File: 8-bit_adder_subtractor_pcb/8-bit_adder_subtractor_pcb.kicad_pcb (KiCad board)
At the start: 2 copper layers, 158.7 x 142 mm, 86 parts, among them J1 Barrel_Jack, SW1 SW_DPDT_x2, SW10 SW_DPDT_x2, SW11 SW_DPDT_x2, SW12 SW_DPDT_x2, SW13 SW_DPDT_x2, SW14 SW_DPDT_x2, SW15 SW_DPDT_x2, SW16 SW_DPDT_x2, SW17 SW_DPDT_x2, SW2 SW_DPDT_x2, SW3 SW_DPDT_x2, SW4 SW_DPDT_x2, SW5 SW_DPDT_x2, SW6 SW_DPDT_x2, SW7 SW_DPDT_x2, SW8 SW_DPDT_x2, SW9 SW_DPDT_x2, U1 74LS86, U10 74LS86, U11 74LS08, U12 74LS32, U2 74LS86, U3 74LS08, U4 74LS08, U5 74LS32, U6 74LS86, U7 74LS86, U8 74LS86, U9 74LS08

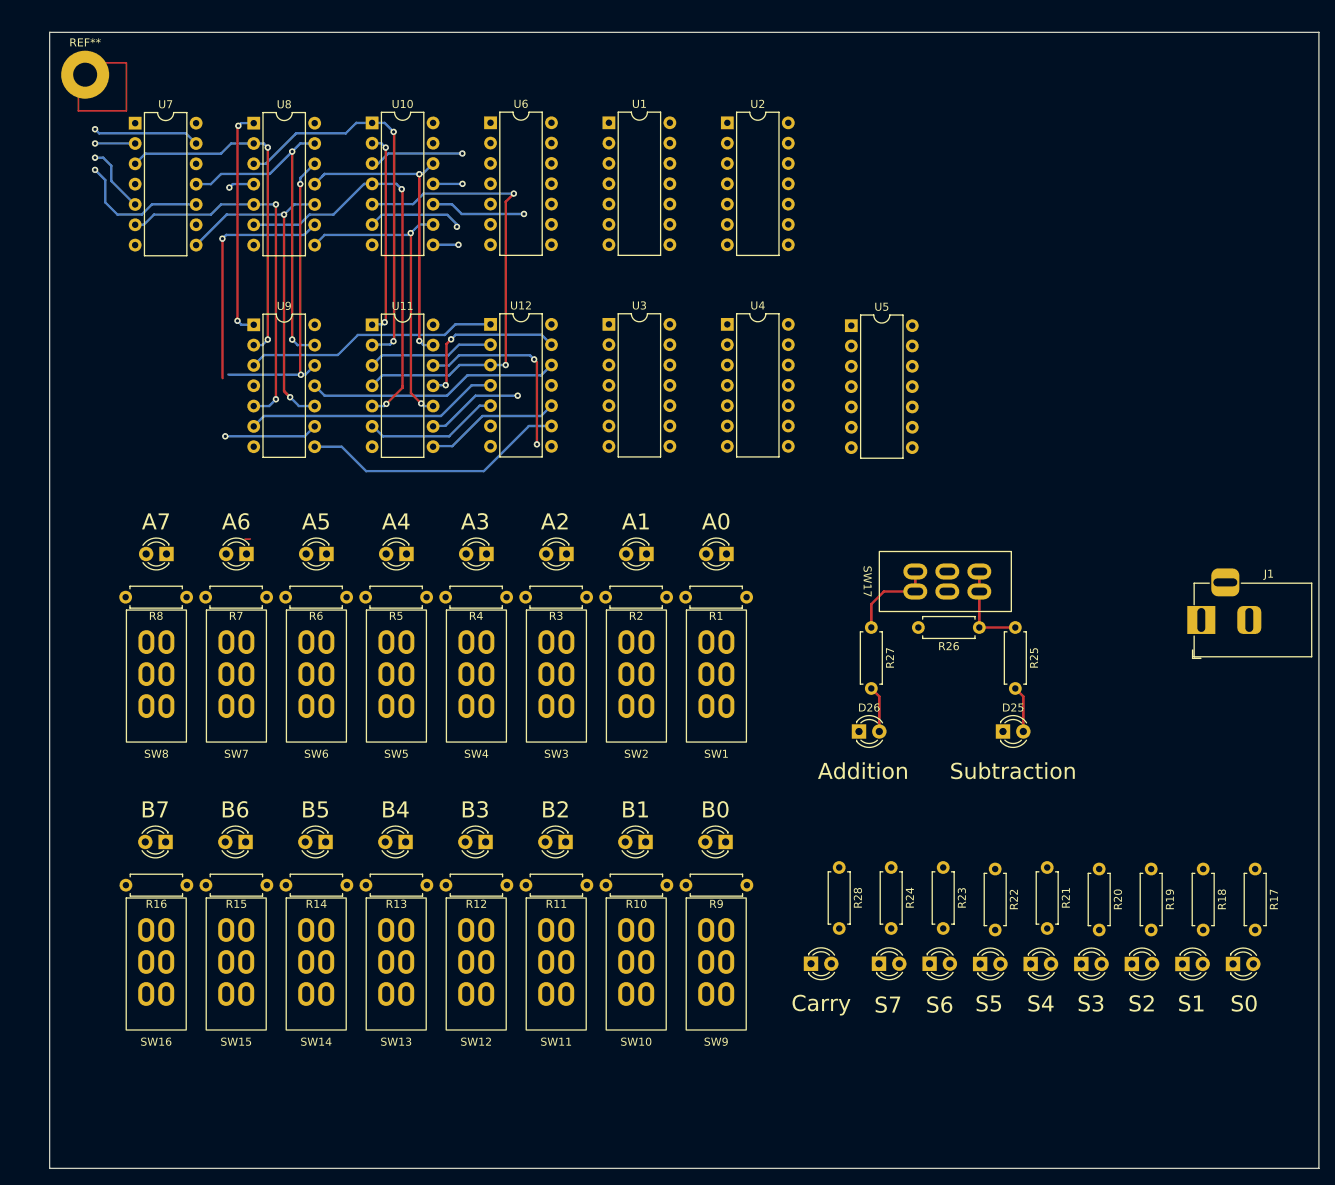
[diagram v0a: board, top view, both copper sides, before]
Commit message: Edited the Silkscreen for LAB448
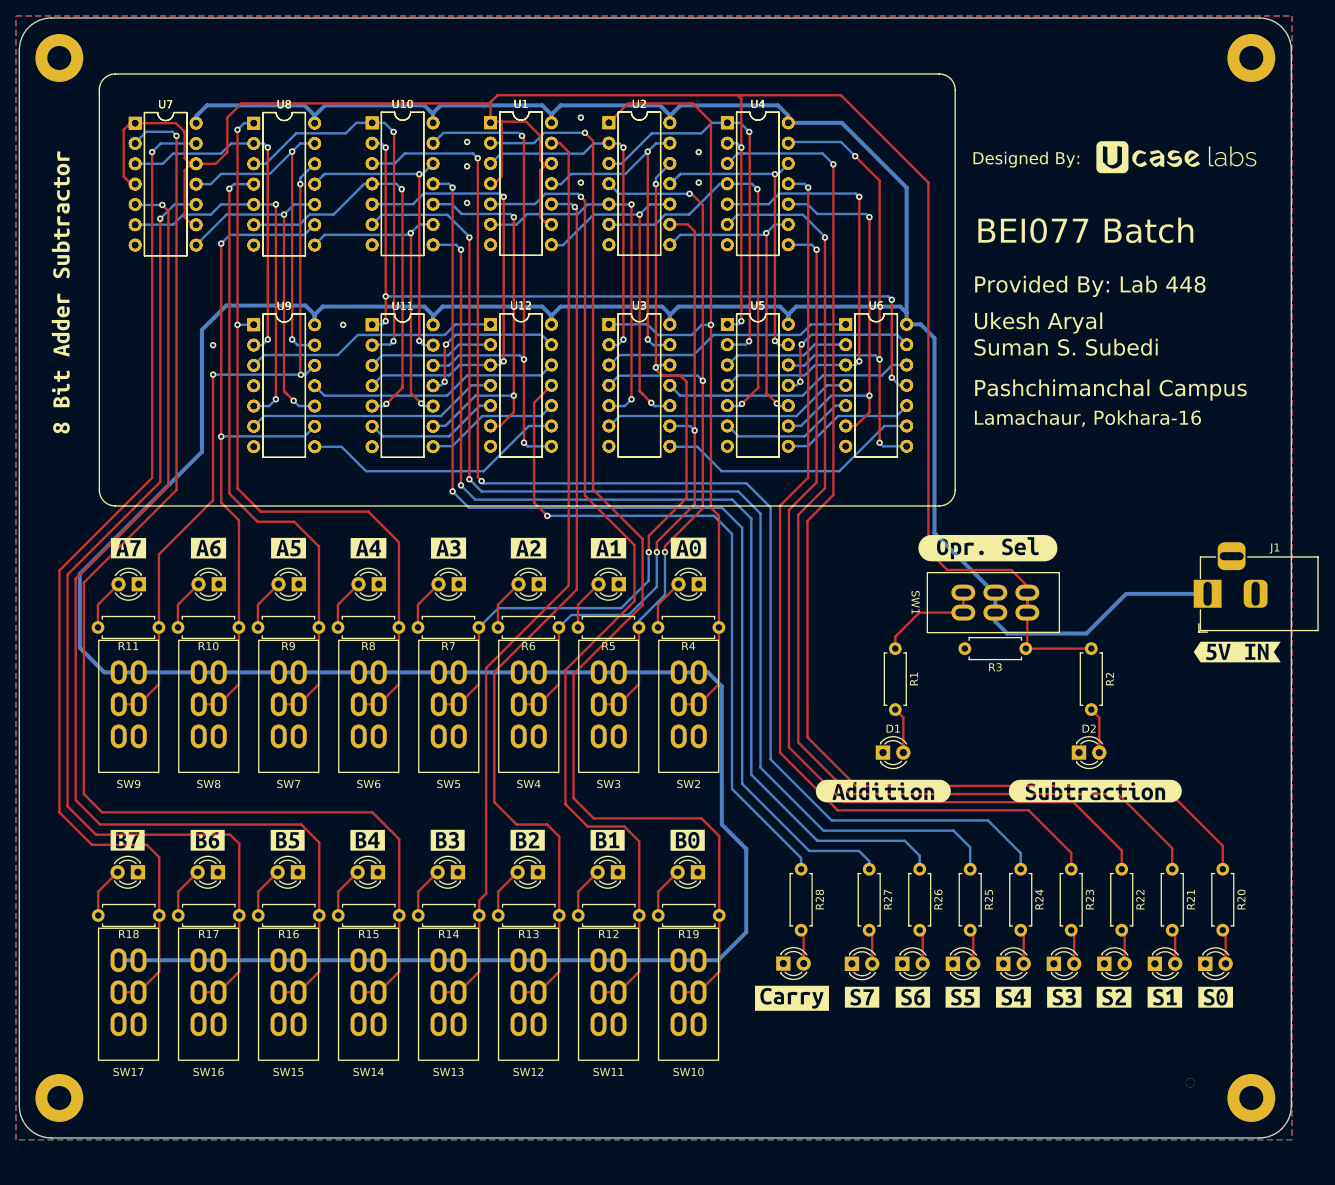
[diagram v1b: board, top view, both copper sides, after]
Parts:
- removed the REF** at (20.7, 15.5)
- added G***: LOGO, Assets:logo, F.Cu at (157.1, 26.2)
- added G***: LOGO, Assets:logo, B.Cu at (150.0, 18.4)
- added H1: MountingHole_Pad, MountingHole:MountingHole_3mm_Pad, F.Cu at (17.5, 13.4)
- added H2: MountingHole_Pad, MountingHole:MountingHole_3mm_Pad, F.Cu at (166.5, 13.4)
- added H3: MountingHole_Pad, MountingHole:MountingHole_3mm_Pad, F.Cu at (166.5, 143.4)
- added H4: MountingHole_Pad, MountingHole:MountingHole_3mm_Pad, F.Cu at (17.5, 143.4)
- added REF**: JLCPC_1.152 Tooling hole, Assets:JLCPC_1.152 Tooling hole, F.Cu at (159.4, 144.6)
- added U1: 74LS86, Package_DIP:DIP-14_W7.62mm, F.Cu at (71.4, 21.6)
- added U10: 74LS86, Package_DIP:DIP-14_W7.62mm, F.Cu at (56.6, 21.6)
- added U11: 74LS08, Package_DIP:DIP-14_W7.62mm, F.Cu at (56.6, 46.8)
- added U12: 74LS32, Package_DIP:DIP-14_W7.62mm, F.Cu at (71.4, 46.8)
- added U2: 74LS86, Package_DIP:DIP-14_W7.62mm, F.Cu at (86.2, 21.6)
- added U3: 74LS08, Package_DIP:DIP-14_W7.62mm, F.Cu at (86.2, 46.8)
- added U4: 74LS86, Package_DIP:DIP-14_W7.62mm, F.Cu at (101.0, 21.6)
- added U5: 74LS08, Package_DIP:DIP-14_W7.62mm, F.Cu at (101.0, 46.8)
- added U6: 74LS32, Package_DIP:DIP-14_W7.62mm, F.Cu at (115.8, 46.8)
- added U7: 74LS86, Package_DIP:DIP-14_W7.62mm, F.Cu at (27.0, 21.6)
- added U8: 74LS86, Package_DIP:DIP-14_W7.62mm, F.Cu at (41.8, 21.6)
- added U9: 74LS08, Package_DIP:DIP-14_W7.62mm, F.Cu at (41.8, 46.8)
- added kibuzzard-6723279E: G***, kibuzzard-6723279E, F.Cu at (86.2, 74.7)
- added kibuzzard-672327BC: G***, kibuzzard-672327BC, F.Cu at (26.2, 74.7)
- added kibuzzard-672327C5: G***, kibuzzard-672327C5, F.Cu at (36.2, 74.7)
- added kibuzzard-672327D0: G***, kibuzzard-672327D0, F.Cu at (46.2, 74.7)
- added kibuzzard-672327D8: G***, kibuzzard-672327D8, F.Cu at (56.2, 74.7)
- added kibuzzard-672327DE: G***, kibuzzard-672327DE, F.Cu at (66.2, 74.7)
- added kibuzzard-672327E5: G***, kibuzzard-672327E5, F.Cu at (76.2, 74.7)
- added kibuzzard-672327EF: G***, kibuzzard-672327EF, F.Cu at (96.2, 74.7)
- added kibuzzard-6723280D: G***, kibuzzard-6723280D, F.Cu at (120.5, 105.1)
- added kibuzzard-67232848: G***, kibuzzard-67232848, F.Cu at (147.0, 105.1)
- added kibuzzard-6723CCFE: G***, kibuzzard-6723CCFE, F.Cu at (26.0, 111.2)
- added kibuzzard-6723CD06: G***, kibuzzard-6723CD06, F.Cu at (36.0, 111.2)
- added kibuzzard-6723CD0E: G***, kibuzzard-6723CD0E, F.Cu at (46.0, 111.2)
- added kibuzzard-6723CD14: G***, kibuzzard-6723CD14, F.Cu at (56.0, 111.2)
- added kibuzzard-6723CD1A: G***, kibuzzard-6723CD1A, F.Cu at (66.0, 111.2)
- added kibuzzard-6723CD21: G***, kibuzzard-6723CD21, F.Cu at (76.0, 111.2)
- added kibuzzard-6723CD27: G***, kibuzzard-6723CD27, F.Cu at (86.0, 111.2)
- added kibuzzard-6723CD2D: G***, kibuzzard-6723CD2D, F.Cu at (96.0, 111.2)
- added kibuzzard-6723D2BC: G***, kibuzzard-6723D2BC, F.Cu at (109.1, 131.0)
- added kibuzzard-6723D2C8: G***, kibuzzard-6723D2C8, F.Cu at (117.8, 130.9)
- added kibuzzard-6723D2CE: G***, kibuzzard-6723D2CE, F.Cu at (124.2, 130.9)
- added kibuzzard-6723D2D3: G***, kibuzzard-6723D2D3, F.Cu at (130.4, 130.9)
- added kibuzzard-6723D2DF: G***, kibuzzard-6723D2DF, F.Cu at (136.8, 130.9)
- added kibuzzard-6723D2E6: G***, kibuzzard-6723D2E6, F.Cu at (143.1, 130.9)
- added kibuzzard-6723D2EE: G***, kibuzzard-6723D2EE, F.Cu at (149.3, 130.9)
- added kibuzzard-6723D31B: G***, kibuzzard-6723D31B, F.Cu at (155.7, 130.9)
- added kibuzzard-6723D320: G***, kibuzzard-6723D320, F.Cu at (162.0, 130.9)
- added kibuzzard-6723D341: G***, kibuzzard-6723D341, F.Cu at (133.6, 74.7)
- added kibuzzard-672491A3: G***, kibuzzard-672491A3, F.Cu at (164.7, 87.7)
- added kibuzzard-68098BF2: G***, kibuzzard-68098BF2, F.Cu at (17.7, 42.7)
- moved D2 9.86 mm to (145.0, 100.3)
- moved R2 9.86 mm to (146.5, 87.3)
- moved SW1 6.56 mm to (134.5, 81.5)
- moved R3 6.38 mm to (138.3, 87.3)
- moved SW6 5.13 mm to (56.2, 94.2)
- moved SW7 5.13 mm to (46.2, 94.2)
- moved SW8 5.13 mm to (36.2, 94.2)
- moved SW17 5.13 mm to (26.2, 130.2)
- moved R10 5.13 mm to (40.0, 84.6)
- moved R12 5.13 mm to (90.0, 120.6)
- moved R13 5.13 mm to (80.0, 120.6)
- moved R14 5.13 mm to (70.0, 120.6)
- moved R15 5.13 mm to (60.0, 120.6)
- moved R16 5.13 mm to (50.0, 120.6)
- moved R17 5.13 mm to (40.0, 120.6)
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- renumbered D26 to D1, A7 to D10, B1 to D11, B2 to D12, B3 to D13, B4 to D14, B5 to D15, B6 to D16, B7 to D17, B0 to D18, S0 to D19, D25 to D2, S1 to D20, S2 to D21, S3 to D22, S4 to D23, S5 to D24, S6 to D25, S7 to D26, Carry to D27, A0 to D3, A1 to D4, A2 to D5, A3 to D6, A4 to D7, A5 to D8, A6 to D9, R27 to R1, R7 to R10, R8 to R11, R10 to R12, R11 to R13, R12 to R14, R13 to R15, R14 to R16, R15 to R17, R16 to R18, R9 to R19, R25 to R2, R17 to R20, R18 to R21, R19 to R22, R20 to R23, R21 to R24, R22 to R25, R23 to R26, R24 to R27, R26 to R3, R1 to R4, R2 to R5, R3 to R6, R4 to R7, R5 to R8, R6 to R9, SW17 to SW1, SW9 to SW10, SW10 to SW11, SW11 to SW12, SW12 to SW13, SW13 to SW14, SW14 to SW15, SW15 to SW16, SW16 to SW17, SW1 to SW2, SW2 to SW3, SW3 to SW4, SW4 to SW5, SW5 to SW6, SW6 to SW7, SW7 to SW8, SW8 to SW9, U6 to U1, U1 to U2, U2 to U4, U4 to U5, U5 to U6
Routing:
- net VCC: track 0.00 -> 541.3 mm
- net SL: track 11.5 -> 275.9 mm, vias 0 -> 2
- net B4: track 4.96 -> 157.6 mm
- net S4: track 11.8 -> 161.6 mm, vias 1 -> 2
- net S0: track 0.00 -> 147.7 mm, vias 0 -> 1
- net B0: track 0.00 -> 145.3 mm, vias 0 -> 1
- net S5: track 11.9 -> 147.1 mm, vias 1 -> 2
- net S1: track 0.00 -> 133.2 mm, vias 0 -> 1
- net B5: track 8.49 -> 137.9 mm
- net S7: track 3.68 -> 131.6 mm, vias 1 -> 2
- net B1: track 0.00 -> 127.8 mm, vias 0 -> 1
- net S6: track 3.18 -> 130.2 mm, vias 1 -> 2
- net S3: track 0.00 -> 118.4 mm, vias 0 -> 1
- net S2: track 0.00 -> 116.7 mm, vias 0 -> 1
- net B3: track 0.00 -> 115.8 mm
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- added copper zone on B.Cu, net GND
- added copper zone on F.Cu, net GND
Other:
- board size 158.7 x 142 mm -> 159 x 140 mm
- board text added: "02/08/2024"
- board text added: "BEI077 Batch"
- board text added: "Designed By:"
- board text added: "Lamachaur, Pokhara-16"
- board text added: "Pashchimanchal Campus"
- board text added: "Provided By: Lab 448"
- board text added: "Suman S. Subedi"
- board text added: "Ukesh Aryal"
- board text added: "V1.0"
